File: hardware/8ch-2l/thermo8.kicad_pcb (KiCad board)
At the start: 2 copper layers, 150 x 154 mm, 267 parts, among them J101 TC CH1-4, J102 TC CH5-8, J401 ENGINE REF FEED/SENSE, J501 AVR ISP, J502 LCD 20x4 HEADER, J503 PANEL BUTTONS, J601 24V IN, J701 TRIP C-NO-NC, J702 ALM C-NO-NC, J703 RS485 A B GND, K701 G6K-2F-Y DC5, K702 G6K-2F-Y DC5, Q401 2N7002, Q402 MMBT3906, Q701 2N7002, Q702 2N7002, SW501 UP, SW502 DOWN, SW503 SET, SW504 ESC, SW505 ACK, U101 AD7124-8BCPZ, U102 TMP126DCKR, U103 TMP126DCKR, U401 B0505S-1WR2, U402 LP2985IM5X-3.3, U403 CA-IS3761HW, U404 CA-IS3761HW, U406 REF3030AIDBZR, U407 MCP6001T-I/OT, U408 TLV7031DBVR, U409 TL431, U411 74LVC1G125, U501 ATmega1284P-AU, U601 LM5164DDAR, U703 ADM2587EBRWZ, Y501 8MHz

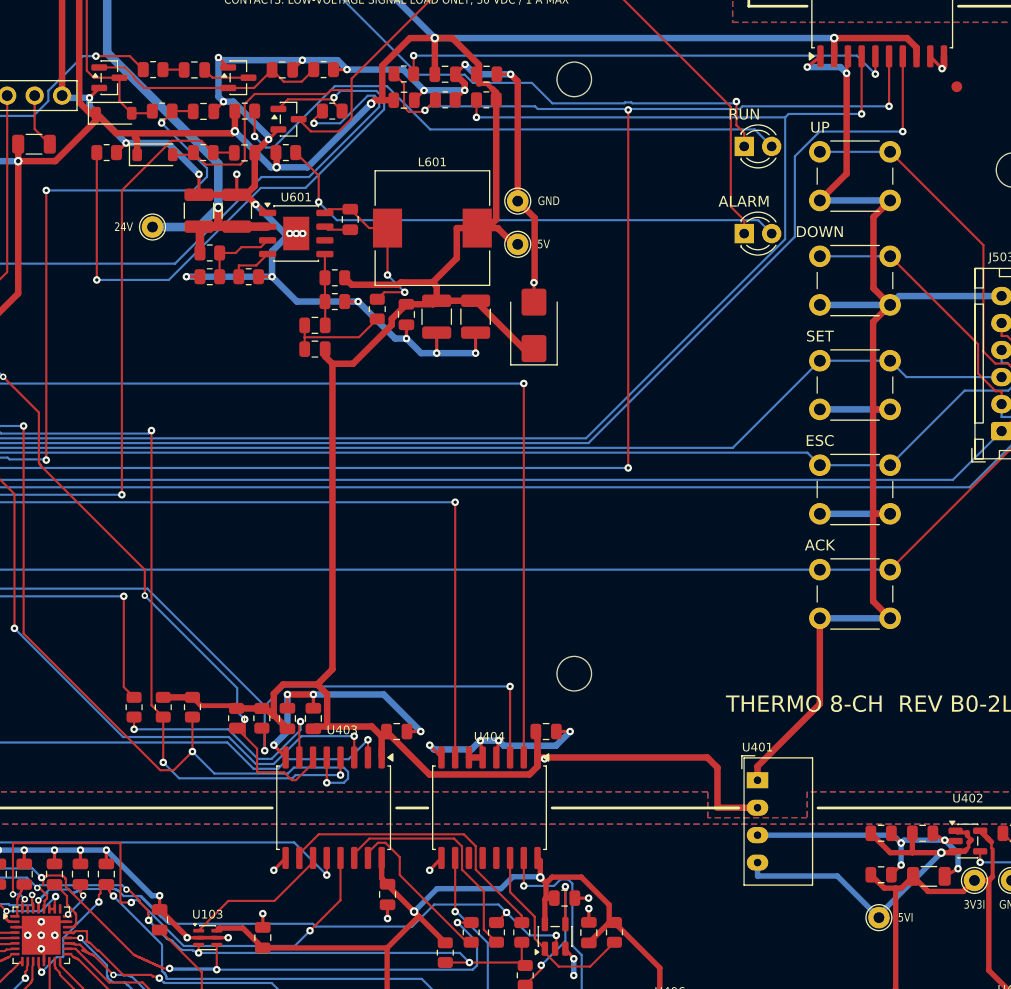
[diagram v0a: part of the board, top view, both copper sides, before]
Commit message: 8ch REV B0-2L: vias out of U703.10 and U101.24 lands (I-131)
DRC 0/0/0 with hole rules as errors, pincaps 0. Release 8ch-revb0-2l-20261019-042949-393f63.

Co-Authored-By: Claude Opus 5.5 <noreply@anthropic.com>
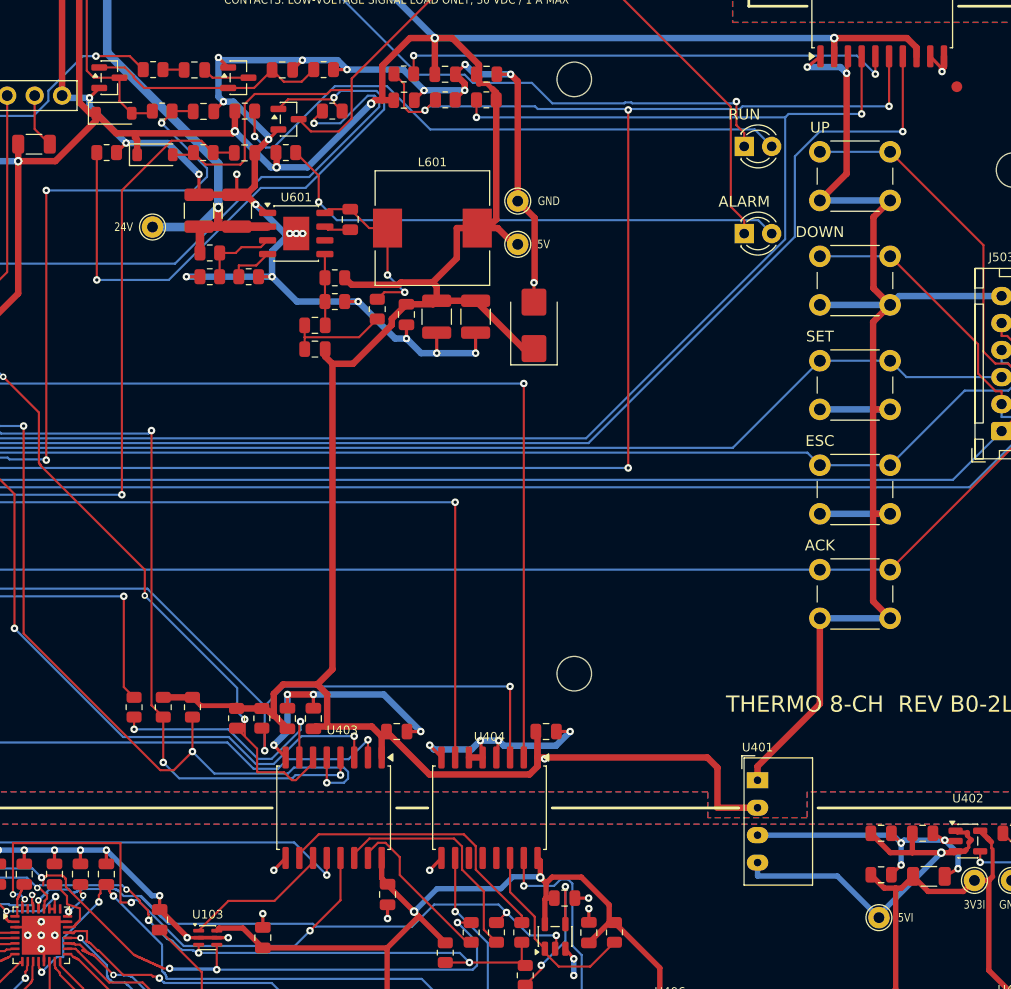
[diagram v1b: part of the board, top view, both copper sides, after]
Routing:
- net /BANK_A_2/REFOUT_A: track 4.33 -> 4.99 mm
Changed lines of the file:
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@@
 	)
 	(segment
+		(start 139.379 35.5768)
+		(end 139.379 35.85)
+		(width 0.6)
+		(layer "F.Cu")
+		(net "GND")
+	)
+	(segment
 		(start 134.5769 57.4445)
 		(end 133.0352 55.9028)
@@
 	)
 	(via
-		(at 139.379 35.5768)
-		(size 0.7)
-		(drill 0.3)
-		(layers "F.Cu" "B.Cu")
-		(net "GND")
-	)
-	(via
 		(at 91.9667 98.1896)
 		(size 0.7)
@@
 	)
 	(via
+		(at 139.379 35.85)
+		(size 0.7)
+		(drill 0.3)
+		(layers "F.Cu" "B.Cu")
+		(net "GND")
+	)
+	(via
 		(at 80.2154 50.8358)
 		(size 0.7)
@@
 	)
 	(segment
-		(start 59.25 113.9)
-		(end 59.25 114.7)
-		(width 0.2)
-		(layer "F.Cu")
-		(net "/BANK_A_2/REFOUT_A")
-	)
-	(segment
 		(start 59.15 114.9)
 		(end 59.1 114.95)
@@
 	)
 	(segment
-		(start 58.4 112.9)
-		(end 58.45 112.95)
-		(width 0.2)
-		(layer "F.Cu")
-		(net "/BANK_A_2/REFOUT_A")
-	)
-	(segment
-		(start 58.45 112.95)
-		(end 58.45 113)
+		(start 59.6 113.3)
+		(end 59.6 114.35)
 		(width 0.2)
 		(layer "F.Cu")
@@
 	)
 	(segment
-		(start 58.45 113)
-		(end 59.2 113.75)
+		(start 58.4 112.9)
+		(end 59.6 113.3)
 		(width 0.2)
 		(layer "F.Cu")
@@
 	)
 	(segment
-		(start 59.2 113.75)
-		(end 59.2 113.85)
+		(start 59.6 114.35)
+		(end 59.25 114.7)
 		(width 0.2)
 		(layer "F.Cu")
@@
 	)
 	(segment
-		(start 59.2 113.85)
-		(end 59.25 113.9)
-		(width 0.2)
-		(layer "F.Cu")
-		(net "/BANK_A_2/REFOUT_A")
-	)
-	(segment
 		(start 66.975 113.395)
 		(end 66.975 112.12)
@@
 	)
 	(segment
-		(start 59.9 112.1)
-		(end 59.644 111.844)
+		(start 58.4567 114.031)
+		(end 58.55 113.6)
 		(width 0.2)
 		(layer "F.Cu")
@@
 	)
 	(segment
-		(start 58.5 113.988)
-		(end 58.5 113.85)
-		(width 0.2)
-		(layer "F.Cu")
-		(net "/BANK_A_2/REGCAPA_A")
-	)
-	(segment
-		(start 58.457 114.031)
-		(end 58.5 113.988)
+		(start 59.9 112.1)
+		(end 59.644 111.844)
 		(width 0.2)
 		(layer "F.Cu")
@@
 	)
 	(via
-		(at 58.5 113.85)
-		(size 0.6)
+		(at 58.55 113.6)
+		(size 0.7)
 		(drill 0.3)
 		(layers "F.Cu" "B.Cu")
@@
 	)
 	(segment
-		(start 59.9 112.45)
-		(end 59.9 112.1)
+		(start 58.55 113.6)
+		(end 59.9 112.45)
 		(width 0.2)
 		(layer "B.Cu")
@@
 	)
 	(segment
-		(start 58.5 113.85)
-		(end 59.9 112.45)
+		(start 59.9 112.45)
+		(end 59.9 112.1)
 		(width 0.2)
 		(layer "B.Cu")

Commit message: 8ch-2l: dangling trim and top-only AD7124 bypass repair (AVDD 3.9 mm/0 vias, IOVDD 2.9 mm); re-released 222750
DRC 0/0/0, pincaps 0, holes 0, fill 317/317, MANIFEST 54/54; all parts on top.

Co-Authored-By: Claude Opus 5.5 <noreply@anthropic.com>
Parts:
- moved C194 10.3 mm to (55.1, 110.1)
- moved C197 7.20 mm to (44.8, 110.1)
- moved C196 3.60 mm to (50.8, 113.5), turned to 180 degrees
- moved C193 2.85 mm to (51.6, 110.2)
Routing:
- net /BANK_A_2/TC8_NA: track 55.8 -> 40.6 mm
- net TC2_NA: track 37.7 -> 26.1 mm
- net +3V3_ISO: track 430.8 -> 438.0 mm, vias 24 -> 21
- net /BANK_A_2/TC7_NA: track 33.4 -> 27.3 mm
- net TC5_PA: track 15.4 -> 13.6 mm
- net SCLK_ISO: track 107.3 -> 105.9 mm
- net TC3_NA: track 19.5 -> 18.2 mm
- net /BANK_A_2/REGCAPD_A: track 2.59 -> 3.86 mm
- net DIN_ISO: track 60.6 -> 61.6 mm
- net TC3_PA: track 22.1 -> 21.2 mm, vias 3 -> 2
- net GND_ISO: track 295.4 -> 296.3 mm, vias 69 -> 68
- net TC4_PA: track 16.4 -> 15.6 mm, vias 3 -> 2
- net CS_ADC1_ISO: track 50.4 -> 50.1 mm, vias 4 -> 2
- net +5V: track 532.7 -> 532.8 mm, vias 12 -> 11
